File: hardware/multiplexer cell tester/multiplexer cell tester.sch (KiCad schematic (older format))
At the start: 11 parts, among them J1 Conn_01x10_Female, J2 Conn_01x10_Female, U1 SN74LVC1G14DRL

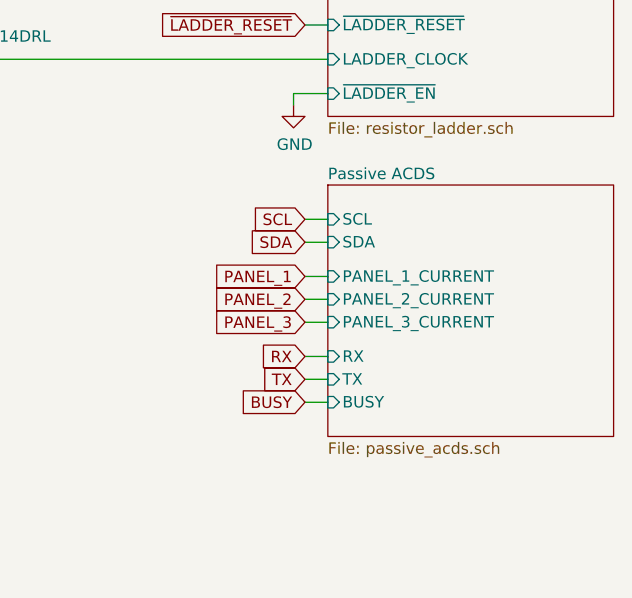
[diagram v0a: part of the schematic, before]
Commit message: Updating curve tracer
- Remove unused circuits
- Update gerbers and renders
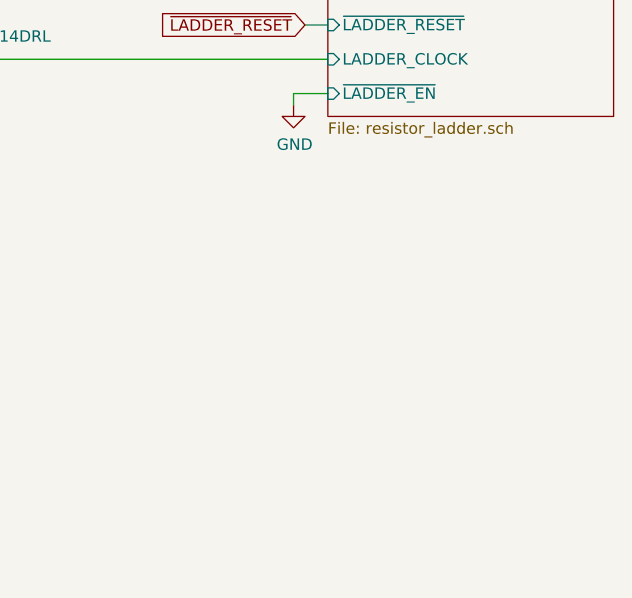
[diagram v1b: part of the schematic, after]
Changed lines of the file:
@@
 $Descr A4 11693 8268
 encoding utf-8
-Sheet 1 5
+Sheet 1 4
 Title "IV Curve Tracer for Ossila AM1.5 Solar Simulator"
-Date "2023-07-08"
+Date "2023-08-20"
 Rev "A"
 Comp "Aerospace eXperimental Payloads | UNL Aerospace Club"
@@
 Text GLabel 2700 4550 2    50   Input ~ 0
 LADDER_CLOCK
-$Sheet
-S 8300 4550 1250 1100
-U 64A6B33A
-F0 "Passive ACDS" 50
-F1 "passive_acds.sch" 50
-F2 "SCL" I L 8300 4700 50
-F3 "SDA" I L 8300 4800 50
-F4 "PANEL_1_CURRENT" I L 8300 4950 50
-F5 "PANEL_2_CURRENT" I L 8300 5050 50
-F6 "PANEL_3_CURRENT" I L 8300 5150 50
-F7 "RX" I L 8300 5300 50
-F8 "TX" I L 8300 5400 50
-F9 "BUSY" I L 8300 5500 50
-$EndSheet
-Text GLabel 8200 4800 0    50   Input ~ 0
-SDA
-Text GLabel 8200 4700 0    50   Input ~ 0
-SCL
-Wire Wire Line
-	8200 4700 8300 4700
-Wire Wire Line
-	8300 4800 8200 4800
-Text GLabel 8200 5300 0    50   Input ~ 0
-RX
-Text GLabel 8200 5400 0    50   Input ~ 0
-TX
-Text GLabel 8200 5500 0    50   Input ~ 0
-BUSY
-Text GLabel 8200 4950 0    50   Input ~ 0
-PANEL_1
-Text GLabel 8200 5050 0    50   Input ~ 0
-PANEL_2
-Text GLabel 8200 5150 0    50   Input ~ 0
-PANEL_3
-Wire Wire Line
-	8200 5500 8300 5500
-Wire Wire Line
-	8300 5400 8200 5400
-Wire Wire Line
-	8200 5300 8300 5300
-Wire Wire Line
-	8300 5150 8200 5150
-Wire Wire Line
-	8200 5050 8300 5050
-Wire Wire Line
-	8200 4950 8300 4950
 Text GLabel 2400 4050 2    50   Input ~ 0
 RX

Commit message: Finalized curve tracer
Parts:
- removed R3, R7: 100, Resistor_SMD:R_0603_1608Metric, symbol Device:R
- removed U1: SN74LVC1G14DRL, Package_TO_SOT_SMD:SOT-23-5, symbol 74xGxx:SN74LVC1G14DRL
- added R33: 100, Resistor_SMD:R_0603_1608Metric, symbol Device:R
- added R34, R35: 4k7, Resistor_SMD:R_0603_1608Metric, symbol Device:R
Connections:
- net +3V3: now also R34.1, R35.1
- net PANEL_1: no longer names the net of J1.6 (Pin_6)
- net PANEL_1: now also R33.1
- net PANEL_2: no longer names the net of J2.3 (Pin_3)
- net PANEL_3: no longer names the net of J2.2 (Pin_2)
- net RX: no longer names the net of J1.3 (Pin_3)
- net SCL renamed Perovskite Switches/SCL
- net Perovskite Switches/SCL: now also R34.2
- net SDA renamed Perovskite Switches/SDA
- net Perovskite Switches/SDA: now also R35.2
- net TX: no longer names the net of J1.4 (Pin_4)
- new net LADDER_UD: R33.2
- no-connect marks 2 -> 8
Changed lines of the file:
@@
 Title "IV Curve Tracer for Ossila AM1.5 Solar Simulator"
 Date "2023-08-20"
-Rev "A"
+Rev "B"
 Comp "Aerospace eXperimental Payloads | UNL Aerospace Club"
 Comment1 "Copyright (c) 2023"
@@
 $EndDescr
 $Sheet
-S 4800 1650 1550 1150
+S 4800 1650 1550 1250
 U 648F7944
 F0 "Perovskite Switches" 50
 F1 "switcher.sch" 50
 F2 "POSITIVE_OUTPUT" I R 6350 1900 50
-F3 "NEGATIVE_OUTPUT" I L 4800 2600 50
+F3 "NEGATIVE_OUTPUT" I L 4800 2500 50
 F4 "10-19_CLOCK" I L 4800 1900 50
 F5 "ENABLE_PANEL_SWITCH" I L 4800 2050 50
 F6 "RESET_PANEL_SWITCH" I L 4800 2200 50
 F7 "REVERSE_BIAS" I L 4800 2350 50
+F8 "SDA" I L 4800 2750 50
+F9 "SCL" I L 4800 2650 50
 $EndSheet
 $Sheet
@@
 F4 "LADDER_CLOCK" I L 8300 4000 50
 F5 "~LADDER_RESET" I L 8300 3850 50
-F6 "LADDER_LATCH" I L 8300 3700 50
+F6 "LADDER_UD" I L 8300 3700 50
 $EndSheet
 $Comp
@@
 $EndComp
 $Comp
-L Device:R R?
-U 1 1 64966A4B
-P 2550 5400
-AR Path="/6313FC31/64966A4B" Ref="R?"  Part="1"
-AR Path="/64966A4B" Ref="R7"  Part="1"
-AR Path="/648F7944/64966A4B" Ref="R?"  Part="1"
-F 0 "R7" V 2550 4950 50  0000 C CNN
-F 1 "100" V 2550 5400 50  0000 C CNN
-F 2 "Resistor_SMD:R_0603_1608Metric" V 2480 5400 50  0001 C CNN
-F 3 "~" H 2550 5400 50  0001 C CNN
-	1    2550 5400
-	0    1    1    0
-$EndComp
-$Comp
 L Device:Ferrite_Bead FB?
 U 1 1 64966A51
@@
 	-1   0    0    -1
 $EndComp
-Text GLabel 2400 4750 2    50   Input ~ 0
-SDA
-Text GLabel 2400 4650 2    50   Input ~ 0
-SCL
 $Comp
 L Device:R R?
@@
 	0    1    1    0
 $EndComp
-Text GLabel 2700 5400 2    50   Input ~ 0
-REVERSE_BIAS
-$Sheet
-S 6600 1650 1500 1750
-U 64A4749F
-F0 "Curve Tracer" 50
-F1 "curve_tracer.sch" 50
-F2 "PANEL_VOLTAGE" I L 6600 1900 50
-F3 "LADDER_VOLTAGE" I R 8100 1900 50
-F4 "READ_CURRENT" I L 6600 3050 50
-F5 "READ_VOLTAGE" I L 6600 3200 50
-$EndSheet
 Wire Wire Line
 	8100 1900 8300 1900
@@
 L power:GND #PWR?
 U 1 1 64A640C4
-P 4650 2650
+P 4650 2500
 AR Path="/6313FC31/64A640C4" Ref="#PWR?"  Part="1"
 AR Path="/64A640C4" Ref="#PWR0103"  Part="1"
 AR Path="/648F7944/64A640C4" Ref="#PWR?"  Part="1"
-F 0 "#PWR0103" H 4650 2400 50  0001 C CNN
-F 1 "GND" H 4655 2477 50  0000 C CNN
-F 2 "" H 4650 2650 50  0001 C CNN
-F 3 "" H 4650 2650 50  0001 C CNN
-	1    4650 2650
-	1    0    0    -1
-$EndComp
-Wire Wire Line
-	4800 2600 4650 2600
-Wire Wire Line
-	4650 2600 4650 2650
+F 0 "#PWR0103" H 4650 2250 50  0001 C CNN
+F 1 "GND" H 4655 2327 50  0000 C CNN
+F 2 "" H 4650 2500 50  0001 C CNN
+F 3 "" H 4650 2500 50  0001 C CNN
+	1    4650 2500
+	0    1    1    0
+$EndComp
 Wire Wire Line
 	4700 2350 4800 2350
@@
 Text GLabel 8200 3850 0    50   Input ~ 0
 ~LADDER_RESET
-Text GLabel 6050 4000 0    50   Input ~ 0
+Text GLabel 8200 4000 0    50   Input ~ 0
 LADDER_CLOCK
 Wire Wire Line
@@
 Text GLabel 2700 4550 2    50   Input ~ 0
 LADDER_CLOCK
-Text GLabel 2400 4050 2    50   Input ~ 0
-RX
-Text GLabel 2400 4150 2    50   Input ~ 0
-TX
-Text GLabel 2700 5000 2    50   Input ~ 0
-BUSY
-Text GLabel 2400 4350 2    50   Input ~ 0
-PANEL_1
-Text GLabel 2400 5700 2    50   Input ~ 0
-PANEL_2
-Text GLabel 2400 5800 2    50   Input ~ 0
-PANEL_3
-NoConn ~ 2400 5500
-NoConn ~ 2400 5600
 $Comp
 L power:GND #PWR?
@@
 $Comp
 L Device:R R?
-U 1 1 64B7E372
-P 2550 5000
-AR Path="/6313FC31/64B7E372" Ref="R?"  Part="1"
-AR Path="/64B7E372" Ref="R3"  Part="1"
-AR Path="/648F7944/64B7E372" Ref="R?"  Part="1"
-F 0 "R3" V 2550 5450 50  0000 C CNN
-F 1 "100" V 2550 5000 50  0000 C CNN
-F 2 "Resistor_SMD:R_0603_1608Metric" V 2480 5000 50  0001 C CNN
-F 3 "~" H 2550 5000 50  0001 C CNN
-	1    2550 5000
-	0    -1   -1   0
-$EndComp
-$Comp
-L Device:R R?
 U 1 1 64B7F6B2
 P 2550 4450
@@
 $EndComp
 $Comp
-L 74xGxx:SN74LVC1G14DRL U?
-U 1 1 64BA669B
-P 6400 3700
-AR Path="/648F7944/64BA669B" Ref="U?"  Part="1"
-AR Path="/64BA669B" Ref="U1"  Part="1"
-F 0 "U1" H 6450 3600 50  0000 L CNN
-F 1 "SN74LVC1G14DRL" H 6450 3500 50  0000 L CNN
-F 2 "Package_TO_SOT_SMD:SOT-23-5" H 6400 3450 50  0001 C CNN
-F 3 "http://www.ti.com/lit/ds/symlink/sn74lvc1g14.pdf" H 6400 3700 50  0001 C CNN
-	1    6400 3700
-	1    0    0    -1
-$EndComp
-$Comp
-L power:GND #PWR?
-U 1 1 64BA6AF4
-P 6400 4050
-AR Path="/6313FC31/64BA6AF4" Ref="#PWR?"  Part="1"
-AR Path="/64BA6AF4" Ref="#PWR0105"  Part="1"
-AR Path="/648F7944/64BA6AF4" Ref="#PWR?"  Part="1"
-F 0 "#PWR0105" H 6400 3800 50  0001 C CNN
-F 1 "GND" H 6405 3877 50  0000 C CNN
-F 2 "" H 6400 4050 50  0001 C CNN
-F 3 "" H 6400 4050 50  0001 C CNN
-	1    6400 4050
-	1    0    0    -1
-$EndComp
-$Comp
-L power:+3V3 #PWR?
-U 1 1 64BA6EDC
-P 6400 3500
-AR Path="/6313FC31/64BA6EDC" Ref="#PWR?"  Part="1"
-AR Path="/64BA6EDC" Ref="#PWR0106"  Part="1"
-AR Path="/648F7944/64BA6EDC" Ref="#PWR?"  Part="1"
-F 0 "#PWR0106" H 6400 3350 50  0001 C CNN
-F 1 "+3V3" H 6415 3673 50  0000 C CNN
-F 2 "" H 6400 3500 50  0001 C CNN
-F 3 "" H 6400 3500 50  0001 C CNN
-	1    6400 3500
-	1    0    0    -1
-$EndComp
-Wire Wire Line
-	6050 4000 6150 4000
-Wire Wire Line
-	6700 3700 8300 3700
-Wire Wire Line
-	6400 3900 6400 4050
-Wire Wire Line
-	6200 3700 6150 3700
-Wire Wire Line
-	6150 3700 6150 4000
-Connection ~ 6150 4000
-Wire Wire Line
-	6150 4000 8300 4000
-$Comp
 L Connector:Conn_01x10_Female J?
 U 1 1 64966A6B
@@
 	-1   0    0    1
 $EndComp
+Text GLabel 8200 3700 0    50   Input ~ 0
+LADDER_UD
+Wire Wire Line
+	8200 3700 8300 3700
+Wire Wire Line
+	8200 4000 8300 4000
+Text GLabel 2700 4350 2    50   Input ~ 0
+LADDER_UD
+$Comp
+L Device:R R?
+U 1 1 65405492
+P 2550 4350
+AR Path="/6313FC31/65405492" Ref="R?"  Part="1"
+AR Path="/65405492" Ref="R33"  Part="1"
+AR Path="/648F7944/65405492" Ref="R?"  Part="1"
+F 0 "R33" V 2550 4800 50  0000 C CNN
+F 1 "100" V 2550 4350 50  0000 C CNN
+F 2 "Resistor_SMD:R_0603_1608Metric" V 2480 4350 50  0001 C CNN
+F 3 "~" H 2550 4350 50  0001 C CNN
+	1    2550 4350
+	0    -1   -1   0
+$EndComp
+$Comp
+L Device:R R?
+U 1 1 65406F8F
+P 3500 4350
+AR Path="/6313FC31/65406F8F" Ref="R?"  Part="1"
+AR Path="/65406F8F" Ref="R34"  Part="1"
+AR Path="/648F7944/65406F8F" Ref="R?"  Part="1"
+F 0 "R34" V 3400 4350 50  0000 C CNN
+F 1 "4k7" V 3500 4350 50  0000 C CNN
+F 2 "Resistor_SMD:R_0603_1608Metric" V 3430 4350 50  0001 C CNN
+F 3 "~" H 3500 4350 50  0001 C CNN
+	1    3500 4350
+	1    0    0    -1
+$EndComp
+$Comp
+L Device:R R?
+U 1 1 65407830
+P 3700 4350
+AR Path="/6313FC31/65407830" Ref="R?"  Part="1"
+AR Path="/65407830" Ref="R35"  Part="1"
+AR Path="/648F7944/65407830" Ref="R?"  Part="1"
+F 0 "R35" V 3600 4350 50  0000 C CNN
+F 1 "4k7" V 3700 4350 50  0000 C CNN
+F 2 "Resistor_SMD:R_0603_1608Metric" V 3630 4350 50  0001 C CNN
+F 3 "~" H 3700 4350 50  0001 C CNN
+	1    3700 4350
+	-1   0    0    -1
+$EndComp
+Wire Wire Line
+	2400 4650 3500 4650
+Wire Wire Line
+	3500 4650 3500 4500
+Wire Wire Line
+	3700 4500 3700 4750
+Connection ~ 3500 4650
+$Comp
+L power:+3V3 #PWR?
+U 1 1 65409252
+P 3500 3350
+AR Path="/6313FC31/65409252" Ref="#PWR?"  Part="1"
+AR Path="/65409252" Ref="#PWR0105"  Part="1"
+AR Path="/648F7944/65409252" Ref="#PWR?"  Part="1"
+F 0 "#PWR0105" H 3500 3200 50  0001 C CNN
+F 1 "+3V3" H 3515 3523 50  0000 C CNN
+F 2 "" H 3500 3350 50  0001 C CNN
+F 3 "" H 3500 3350 50  0001 C CNN
+	1    3500 3350
+	1    0    0    -1
+$EndComp
+$Comp
+L power:+3V3 #PWR?
+U 1 1 6540991E
+P 3700 3350
+AR Path="/6313FC31/6540991E" Ref="#PWR?"  Part="1"
+AR Path="/6540991E" Ref="#PWR0106"  Part="1"
+AR Path="/648F7944/6540991E" Ref="#PWR?"  Part="1"
+F 0 "#PWR0106" H 3700 3200 50  0001 C CNN
+F 1 "+3V3" H 3715 3523 50  0000 C CNN
+F 2 "" H 3700 3350 50  0001 C CNN
+F 3 "" H 3700 3350 50  0001 C CNN
+	1    3700 3350
+	1    0    0    -1
+$EndComp
+Wire Wire Line
+	3500 3350 3500 4200
+Connection ~ 3700 4750
+Wire Wire Line
+	2400 4750 3700 4750
+Wire Wire Line
+	3700 4200 3700 3350
+NoConn ~ 2400 4050
+NoConn ~ 2400 4150
+NoConn ~ 2400 5800
+NoConn ~ 2400 5700
+NoConn ~ 2400 5600
+NoConn ~ 2400 5500
+$Sheet
+S 6600 1650 1500 1750
+U 64A4749F
+F0 "Curve Tracer" 50
+F1 "curve_tracer.sch" 50
+F2 "PANEL_VOLTAGE" I L 6600 1900 50
+F3 "LADDER_VOLTAGE" I R 8100 1900 50
+F4 "READ_CURRENT" I L 6600 3050 50
+F5 "READ_VOLTAGE" I L 6600 3200 50
+$EndSheet
+Wire Wire Line
+	4650 2500 4800 2500
+Wire Wire Line
+	4000 4650 4000 2650
+Wire Wire Line
+	4000 2650 4800 2650
+Wire Wire Line
+	3500 4650 4000 4650
+Wire Wire Line
+	4100 4750 4100 2750
+Wire Wire Line
+	4100 2750 4800 2750
+Wire Wire Line
+	3700 4750 4100 4750
+NoConn ~ 2400 5000
+NoConn ~ 2400 5400
 $EndSCHEMATC
